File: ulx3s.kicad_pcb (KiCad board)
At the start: 4 copper layers, 139.5 x 91.8 mm, 279 parts, among them IC101 TPD4E001DRLR, IC102 74AUP1G74DC.125, IC103 CD74HC4050PWR, IC104 STM32F769IIT6, IC105 LD1117ADT33TR, IC106 N.C., IC107 IS42S16400J, IC108 AT24C256C-SSHL-B, IC109 TPS2051BDBVR, IC110 TPS61169DCKR, IC111 TPD4E001DRLR, IC112 TSC2007IPW, IC113 N.C., IC114 DP83848CVV_NOPB, J101 503398-1892, J102 67803-8020, J4 CONN_02X03, Q101 N.C., Q102 2N7002, SW101 TL1100CF160Q, SW102 PEC16-2215F-S0024, U1 LFE5U-85F-6BG381C, U10 IS25LP128F-JBLE, U3 TLV62569DBV, U4 TLV62569DBV, U5 TLV62569DBV, X101 DS1024-2*20R0, X102 DS1013-16SSIB1, X103 691322110005, X104 N.C., X105 LMJTAB881243M-L, Y1 FNETHE025, Y101 25MHz, Y102 XTAL016178-85SMX

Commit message: better RGB-OUT
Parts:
- moved Y1 2.45 mm to (153.5, 95.7)
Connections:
- net FTDI_TXDEN renamed LTDC_FROM_FPGA_G2
- LCD101 pad 10: FTDI_nRXLED -> LTDC_FROM_FPGA_R5
- LCD101 pad 18: FTDI_RXD -> LTDC_FROM_FPGA_G5
- LCD101 pad 34: LTDC_FROM_FPGA_DE -> (no net)
- U1 pad E6: (no net) -> LTDC_FROM_FPGA_R3
- U1 pad E9: (no net) -> LTDC_FROM_FPGA_R5
- U1 pad G1: LTDC_FROM_FPGA_R3 -> LTDC_FROM_FPGA_R4
- U1 pad H1: LTDC_FROM_FPGA_G3 -> LTDC_FROM_FPGA_R6
- U1 pad J1: LTDC_FROM_FPGA_R6 -> (no net)
- U1 pad J5: LTDC_FROM_FPGA_R4 -> LTDC_FROM_FPGA_R7
- U1 pad K1: LTDC_FROM_FPGA_R7 -> (no net)
- U1 pad K2: LTDC_FROM_FPGA_G4 -> (no net)
- U1 pad K3: (no net) -> LTDC_FROM_FPGA_G5
- U1 pad K4: LTDC_FROM_FPGA_G6 -> LTDC_FROM_FPGA_G4
- U1 pad K5: (no net) -> LTDC_FROM_FPGA_G3
- U1 pad L1: LTDC_FROM_FPGA_B4 -> LTDC_FROM_FPGA_G7
- U1 pad L4: FTDI_RXD -> LTDC_FROM_FPGA_G6
- U1 pad L5: FTDI_nRXLED -> (no net)
- U1 pad N2: LTDC_FROM_FPGA_B6 -> (no net)
- U1 pad N3: LTDC_FROM_FPGA_B3 -> (no net)
- U1 pad N4: LTDC_FROM_FPGA_G7 -> (no net)
- U1 pad N5: LTDC_FROM_FPGA_DE -> (no net)
- U1 pad P1: LTDC_FROM_FPGA_B7 -> (no net)
- U1 pad P2: (no net) -> LTDC_FROM_FPGA_B3
- U1 pad P4: (no net) -> LTDC_FROM_FPGA_B6
- U1 pad R1: (no net) -> LTDC_FROM_FPGA_B4
- U1 pad T1: (no net) -> LTDC_FROM_FPGA_B7
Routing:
- net (no net): track 433.2 -> 418.6 mm, vias 92 -> 89
- net LTDC_FROM_FPGA_R5: track 0.00 -> 12.6 mm, vias 0 -> 1
- net +2V5: track 103.0 -> 110.3 mm
- net LTDC_FROM_FPGA_R3: track 4.39 -> 11.2 mm, vias 0 -> 1
- net LTDC_FROM_FPGA_R7: track 0.60 -> 7.16 mm, vias 0 -> 1
- net FTDI_nRXLED: track 6.37 -> 0.00 mm, vias 2 -> 0
- net LTDC_FROM_FPGA_G5: track 0.00 -> 5.56 mm, vias 0 -> 2
- net LTDC_FROM_FPGA_VSYNC: track 4.99 -> 0.00 mm, vias 2 -> 0
- net +3V3: track 85.3 -> 80.4 mm
- net FTDI_RXD: track 3.47 -> 0.00 mm, vias 1 -> 0
- net LTDC_FROM_FPGA_G3: track 3.69 -> 6.96 mm, vias 0 -> 1
- net LTDC_FROM_FPGA_R4: track 7.15 -> 4.39 mm, vias 1 -> 0
- net LTDC_FROM_FPGA_G6: track 6.13 -> 3.47 mm, vias 0 -> 1
- net LTDC_FROM_FPGA_G4: track 4.46 -> 5.87 mm
- net CLK_25MHz: track 9.06 -> 7.68 mm
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
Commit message: More fixes
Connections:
- net AUDIO_L0 renamed LTDC_TO_FPGA_DE
- net AUDIO_L1 renamed LTDC_TO_FPGA_B6
- net AUDIO_L2 renamed LTDC_TO_FPGA_G4
- net AUDIO_R0 renamed LTDC_TO_FPGA_G2
- net AUDIO_R2 renamed LTDC_TO_FPGA_B5
- net AUDIO_V2 renamed LTDC_TO_FPGA_B4
- net BTN_D renamed LTDC_FROM_FPGA_VSYNC
- net BTN_L renamed LTDC_FROM_FPGA_HSYNC
- net GN10 renamed LTDC_TO_FPGA_B7
- net GN11 renamed LTDC_TO_FPGA_B3
- net GN9 renamed LTDC_TO_FPGA_R6
- net GP11 renamed LTDC_TO_FPGA_G5
- net GP12 renamed LTDC_TO_FPGA_CLK
- net GP9 renamed LTDC_TO_FPGA_G7
- net LED1 renamed LTDC_TO_FPGA_R7
- net LED2 renamed LTDC_TO_FPGA_HSYNC
- net LED3 renamed LTDC_TO_FPGA_VSYNC
- net LED4 renamed LTDC_TO_FPGA_R4
- net LED6 renamed LTDC_TO_FPGA_R5
- net LED7 renamed LTDC_TO_FPGA_R3
- LCD101 pad 34: (no net) -> LTDC_FROM_FPGA_DE
- U1 pad U17: (no net) -> LTDC_FROM_FPGA_DE
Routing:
- net USER_PROGRAMN: track 10.2 -> 17.4 mm, vias 1 -> 2
- net (no net): track 418.6 -> 412.5 mm, vias 89 -> 87
- net LTDC_FROM_FPGA_DE: track 0.00 -> 5.95 mm, vias 0 -> 2

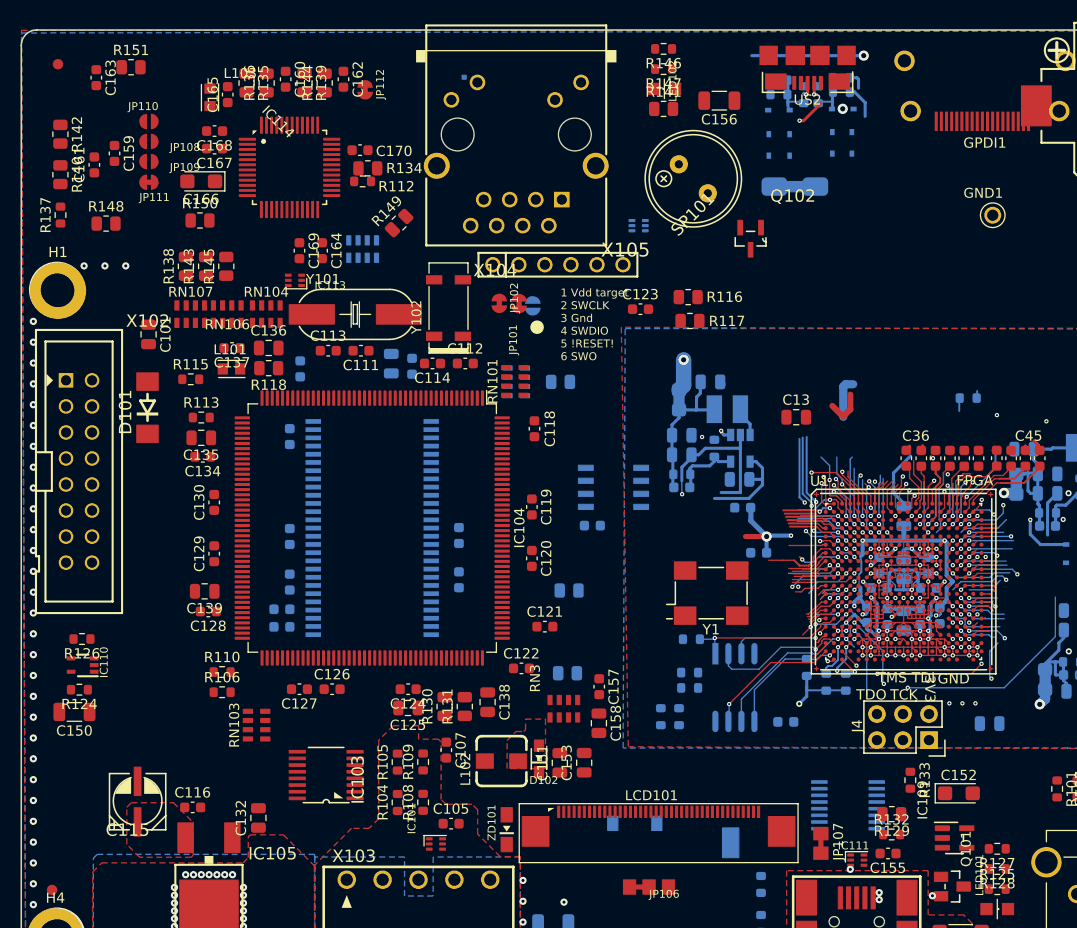
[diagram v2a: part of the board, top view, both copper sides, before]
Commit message: Adding all SPI to FPGA resorting LCD TO FPGA
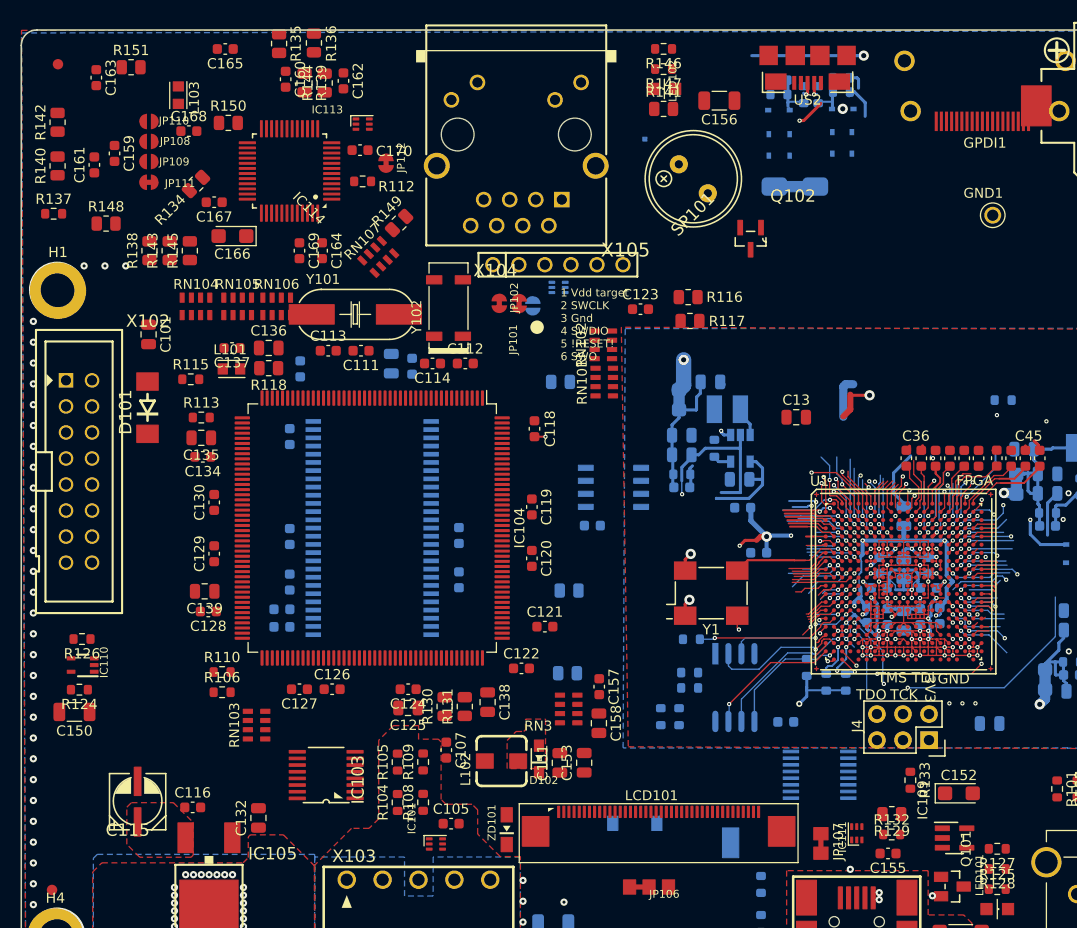
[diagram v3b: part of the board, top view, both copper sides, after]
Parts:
- RN102, RN105: moved to F.Cu
- moved RN107 19.1 mm to (121.0, 62.9), turned to 45 degrees
- moved SH101 18.6 mm to (147.0, 51.4)
- moved R134 16.8 mm to (103.2, 55.7), turned to 225 degrees
- moved IC113 16.6 mm to (119.5, 49.9), turned to 0 degrees
- moved RN105 13.4 mm to (107.3, 67.7), turned to 0 degrees
- moved R150 9.91 mm to (106.3, 49.8)
- moved IC106 9.87 mm to (138.6, 65.8)
- moved RN102 9.23 mm to (142.9, 71.4), turned to 90 degrees
- moved RN101 8.71 mm to (143.0, 75.1)
- moved JP112 7.44 mm to (121.7, 53.7)
- moved RN104 6.90 mm to (103.2, 67.7)
- moved C166 6.14 mm to (106.8, 60.8)
- moved R136 6.05 mm to (114.7, 42.0)
- moved C167 5.23 mm to (105.0, 57.5)
- moved R135 4.98 mm to (111.3, 42.0)
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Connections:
- IC104 pad 123: (no net) -> SPI2_TO_FPGA_IRQ
- IC104 pad 138: (no net) -> SPI5_TO_FPGA_IRQ
- IC104 pad 156: (no net) -> SPI5_TO_FPGA_CSB
- IC104 pad 168: (no net) -> SPI4_TO_FPGA_IRQ
- IC104 pad 4: (no net) -> SPI4_TO_FPGA_MISO
- IC104 pad 87: (no net) -> SPI2_TO_FPGA_MISO
- J101 pad 5: (no net) -> SDMMC1_FROM_FPGA_CK
- J101 pad SW1: (no net) -> SD_FROM_FPGA_DETECT
- RN101 pad 1: (no net) -> SPI4_TO_FPGA_CLK
- RN101 pad 2: (no net) -> SPI4_TO_FPGA_CSB
- RN101 pad 3: (no net) -> SPI4_TO_FPGA_CSA
- RN101 pad 4: (no net) -> SPI4_TO_FPGA_MOSI
- RN102 pad 1: (no net) -> SPI5_TO_FPGA_CSA
- RN102 pad 2: (no net) -> SPI5_TO_FPGA_CLK
- RN102 pad 3: (no net) -> SPI5_TO_FPGA_MISO
- RN102 pad 4: (no net) -> SPI5_TO_FPGA_MOSI
- RN103 pad 4: (no net) -> SPI2_TO_FPGA_CSA
- RN3 pad 1: (no net) -> SPI2_TO_FPGA_CSB
- RN3 pad 2: (no net) -> SPI2_TO_FPGA_CLK
- RN3 pad 3: (no net) -> SPI2_TO_FPGA_MOSI
- U1 pad A2: LTDC_TO_FPGA_G7 -> SPI5_TO_FPGA_CSB
- U1 pad A3: LTDC_TO_FPGA_G2 -> SPI4_TO_FPGA_MISO
- U1 pad A4: (no net) -> SPI4_TO_FPGA_MOSI
- U1 pad A5: (no net) -> SPI4_TO_FPGA_CSB
- U1 pad A6: (no net) -> SPI5_TO_FPGA_MISO
- U1 pad B1: LTDC_TO_FPGA_R6 -> SPI4_TO_FPGA_CSA
- U1 pad B2: LTDC_TO_FPGA_G6 -> LTDC_TO_FPGA_B6
- U1 pad B3: (no net) -> LTDC_TO_FPGA_G2
- U1 pad B4: LTDC_TO_FPGA_B7 -> (no net)
- U1 pad B5: (no net) -> SPI5_TO_FPGA_CSA
- U1 pad C1: LTDC_TO_FPGA_HSYNC -> LTDC_FROM_FPGA_R5
- U1 pad C2: LTDC_TO_FPGA_R7 -> LTDC_TO_FPGA_B7
- U1 pad C3: LTDC_TO_FPGA_G4 -> LTDC_TO_FPGA_R5
- U1 pad C4: LTDC_TO_FPGA_G3 -> SPI4_TO_FPGA_IRQ
- U1 pad D1: LTDC_TO_FPGA_R4 -> LTDC_TO_FPGA_G4
- U1 pad D3: LTDC_TO_FPGA_B6 -> LTDC_TO_FPGA_DE
- U1 pad D5: LTDC_TO_FPGA_B5 -> (no net)
- U1 pad D6: (no net) -> SPI5_TO_FPGA_MOSI
- U1 pad E1: LTDC_TO_FPGA_R5 -> LTDC_TO_FPGA_B3
- U1 pad E2: (no net) -> LTDC_TO_FPGA_R4
- U1 pad E3: LTDC_TO_FPGA_B3 -> LTDC_TO_FPGA_R3
- U1 pad E4: LTDC_TO_FPGA_DE -> LTDC_TO_FPGA_HSYNC
- U1 pad E5: (no net) -> LTDC_TO_FPGA_R6
- U1 pad E9: LTDC_FROM_FPGA_R5 -> LTDC_TO_FPGA_G6
- U1 pad F1: (no net) -> LTDC_TO_FPGA_G7
- U1 pad F2: (no net) -> SPI4_TO_FPGA_CLK
- U1 pad F4: LTDC_TO_FPGA_G5 -> LTDC_TO_FPGA_B4
- U1 pad F5: LTDC_TO_FPGA_B4 -> LTDC_TO_FPGA_B5
- U1 pad G3: LTDC_TO_FPGA_CLK -> LTDC_TO_FPGA_G3
- U1 pad G5: (no net) -> LTDC_TO_FPGA_G5
- U1 pad H2: (no net) -> SDMMC1_FROM_FPGA_CK
- U1 pad H3: LTDC_TO_FPGA_R3 -> LTDC_TO_FPGA_R7
- U1 pad H4: (no net) -> LTDC_TO_FPGA_CLK
- U1 pad H5: (no net) -> SPI5_TO_FPGA_CLK
- U1 pad J1: (no net) -> SDMMC1_FROM_FPGA_CMD
- U1 pad J3: (no net) -> SDMMC1_FROM_FPGA_D0
- U1 pad L16: (no net) -> SPI2_TO_FPGA_CLK
- U1 pad N16: (no net) -> SPI2_TO_FPGA_IRQ
- U1 pad N17: (no net) -> SPI2_TO_FPGA_MISO
- U1 pad N5: (no net) -> SD_FROM_FPGA_DETECT
- U1 pad P16: (no net) -> SPI2_TO_FPGA_CSA
- U1 pad R16: (no net) -> SPI5_TO_FPGA_IRQ
- U1 pad R17: (no net) -> SPI2_TO_FPGA_MOSI
- U1 pad R18: (no net) -> SPI2_TO_FPGA_CSB
- U1 pad U16: (no net) -> I2C1_SDA
- U1 pad U18: (no net) -> I2C1_SCL
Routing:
- net (no net): track 412.5 -> 309.1 mm, vias 87 -> 70
- net +2V5: track 110.3 -> 97.0 mm
- net LTDC_TO_FPGA_B4: track 13.5 -> 4.13 mm, vias 2 -> 1
- net SPI4_TO_FPGA_IRQ: track 0.00 -> 8.87 mm, vias 0 -> 2
- net LTDC_FROM_FPGA_R5: track 12.6 -> 4.15 mm, vias 1 -> 0
- net SPI4_TO_FPGA_CSB: track 0.00 -> 7.84 mm, vias 0 -> 1
- net CLK_25MHz: track 7.68 -> 15.1 mm
- net LTDC_TO_FPGA_G6: track 5.30 -> 12.6 mm, vias 2 -> 1
- net SPI5_TO_FPGA_IRQ: track 0.00 -> 6.95 mm, vias 0 -> 1
- net SPI5_TO_FPGA_CSA: track 0.00 -> 6.23 mm, vias 0 -> 1
- net I2C1_SDA: track 0.00 -> 6.22 mm, vias 0 -> 1
- net 2V5_3V3: track 28.0 -> 34.2 mm, vias 2 -> 3
- net SPI5_TO_FPGA_CSB: track 0.00 -> 6.04 mm, vias 0 -> 1
- net SPI2_TO_FPGA_CSA: track 0.00 -> 5.91 mm, vias 0 -> 1
- net SPI4_TO_FPGA_MISO: track 0.00 -> 5.76 mm, vias 0 -> 1
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- removed copper zone on In2.Cu, net +3V3

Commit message: Partial copied SDRAM routing from BB3
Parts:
- added EEZ_SIGNATURE: SIGNATURESMALL, EEZ DIB MCU r3B4:SIGNATURE_5MM, F.Cu at (-24.1, 57.5)
- added U$1: , EEZ DIB MCU r3B4:RECYCLE_BIN1_8, F.Cu at (-29.1, 67.4)
- added U$2: , EEZ DIB MCU r3B4:CE_5MM, F.Cu at (-18.5, 68.0)
- added U$5: , EEZ DIB MCU r3B4:PB_SMALL, F.Cu at (-30.8, 64.0)
- added U$6: , EEZ DIB MCU r3B4:ESD_SYMBOL, F.Cu at (-39.1, 67.4)
- moved IC108 68.1 mm to (206.0, 57.5)
- moved C120 50.4 mm to (185.7, 84.3), turned to 0 degrees
- moved C119 50.3 mm to (185.7, 79.7), turned to 0 degrees
- moved C118 49.7 mm to (185.0, 70.0)
- moved C146 49.7 mm to (161.3, 71.9)
- moved C143 49.7 mm to (160.5, 90.5)
- moved C149 49.7 mm to (160.5, 88.8)
- moved C145 49.6 mm to (161.3, 81.7)
- moved C144 49.6 mm to (161.3, 86.2)
- moved C121 49.4 mm to (185.9, 90.9)
- moved IC107 49.3 mm to (169.0, 80.9)
- moved IC104 49.3 mm to (169.0, 80.9)
- moved C148 48.6 mm to (176.7, 86.1)
- moved C147 48.6 mm to (176.7, 81.8)
- moved R119 48.0 mm to (186.0, 66.9)
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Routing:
- net (no net): track 309.1 -> 347.9 mm, vias 70 -> 73
- net LTDC_TO_FPGA_R5: track 5.79 -> 39.5 mm, vias 1 -> 2
- net UART_TX/DOUT1: track 0.00 -> 30.8 mm, vias 0 -> 2
- net UART_RX/DIN1: track 0.00 -> 30.7 mm, vias 0 -> 2
- net LTDC_DE: track 0.00 -> 30.0 mm
- net LTDC_TO_FPGA_VSYNC: track 4.88 -> 34.7 mm, vias 0 -> 1
- net LTDC_TO_FPGA_HSYNC: track 6.77 -> 36.3 mm, vias 1 -> 2
- net LTDC_TO_FPGA_G6: track 12.6 -> 42.0 mm, vias 1 -> 2
- net LTDC_TO_FPGA_G4: track 4.02 -> 31.3 mm, vias 0 -> 1
- net +3V3: track 86.0 -> 112.1 mm
- net LTDC_TO_FPGA_R4: track 4.69 -> 29.0 mm, vias 0 -> 1
- net LTDC_TO_FPGA_G2: track 7.04 -> 29.9 mm, vias 1 -> 2
- net FMC_A12: track 0.00 -> 22.3 mm, vias 0 -> 3
- net FMC_SDCKE0: track 0.00 -> 21.5 mm, vias 0 -> 1
- net PWR_DIRECT: track 0.00 -> 21.5 mm, vias 0 -> 1
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
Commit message: Locking logos
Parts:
- moved EEZ_SIGNATURE 125.8 mm to (100.8, 71.8)
- moved U$2 125.8 mm to (106.4, 82.3)
- moved U$1 125.8 mm to (95.9, 81.8)
- moved U$5 125.8 mm to (94.2, 78.4)
- moved U$6 125.8 mm to (85.9, 81.8)

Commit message: Before autorouter
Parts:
- removed U$5: , EEZ DIB MCU r3B4:PB_SMALL
- moved JP102 8.30 mm to (180.3, 64.3)
- moved JP101 5.00 mm to (177.7, 63.5)
- moved JP105 4.42 mm to (177.8, 63.4)
